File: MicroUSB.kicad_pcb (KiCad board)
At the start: 2 copper layers, 13.8 x 16.1 mm, 11 parts, among them J1 USB_OTG, J2 Conn_01x05, Q1 MMBT3904, U1 USBLC6-2SC6

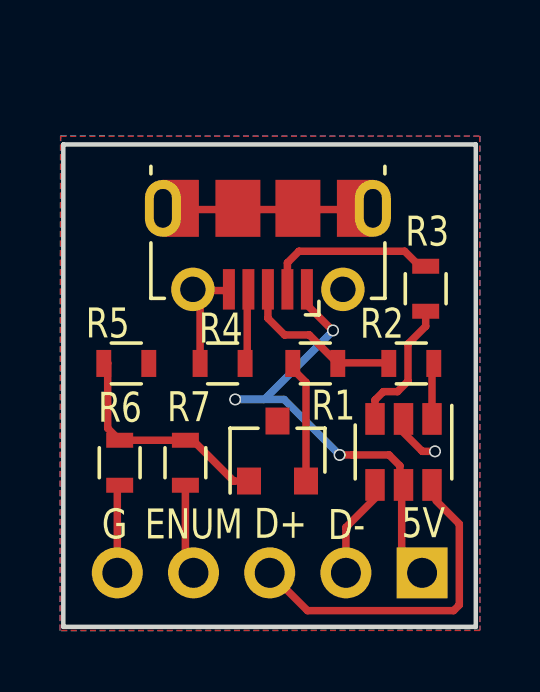
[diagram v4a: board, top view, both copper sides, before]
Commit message: Added a txt V.01 indicated version 1 and added gerber file for panelizing
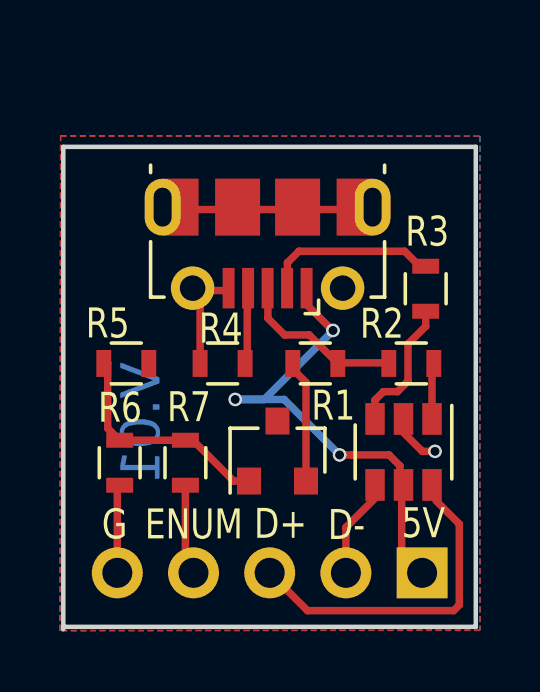
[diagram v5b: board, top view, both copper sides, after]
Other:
- outline, holes or cut-outs redrawn
- net class new added: clearance 0.2, trace_width 0.25, via_dia 0.453, via_drill 0.3
- board text added: "Micro_USB_Conn"
- board text added: "V.01"
- board text removed: "Micro_USB_Connector"
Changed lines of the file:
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@@
     (links 29)
     (no_connects 0)
-    (area 145.684999 109.545 160.555 127.795001)
+    (area 136.700001 107.04 160.555 127.795001)
     (thickness 1.6)
-    (drawings 27)
+    (drawings 28)
     (tracks 85)
     (zones 0)
@@
     (pad_drill 0.85)
     (pad_to_mask_clearance 0.2)
-    (aux_axis_origin 0 0)
+    (aux_axis_origin 144.76 110.82)
     (visible_elements 7FFFFFFF)
     (pcbplotparams
-      (layerselection 0x00030_80000001)
-      (usegerberextensions false)
+      (layerselection 0x0ffff_80000001)
+      (usegerberextensions true)
+      (usegerberattributes true)
       (excludeedgelayer true)
       (linewidth 0.100000)
@@
       (viasonmask false)
       (mode 1)
-      (useauxorigin false)
+      (useauxorigin true)
       (hpglpennumber 1)
       (hpglpenspeed 20)
@@
       (psa4output false)
       (plotreference true)
-      (plotvalue true)
+      (plotvalue false)
       (plotinvisibletext false)
       (padsonsilk false)
@@
       (outputformat 1)
       (mirror false)
-      (drillshape 1)
+      (drillshape 0)
       (scaleselection 1)
-      (outputdirectory ""))
+      (outputdirectory GERBER_MUSB/))
   )
   (net 0 "")
@@
     (add_net "Net-(R3-Pad1)")
   )
+  (net_class new ""
+    (clearance 0.2)
+    (trace_width 0.25)
+    (via_dia 0.453)
+    (via_drill 0.3)
+    (uvia_dia 0.3)
+    (uvia_drill 0.1)
+  )
   (module Connectors_USB:USB_Micro-B_Molex-105017-0001 (layer F.Cu)
-    (at 152.72 113.97 180)
+    (at 152.71 113.93 180)
     (descr http://www.molex.com/pdm_docs/sd/1050170001_sd.pdf)
     (tags "Micro-USB SMD Typ-B")
@@
     )
   )
-  (dimension 16.08 (width 0.3) (layer Eco1.User)
-    (gr_text "16.080 mm" (at 143.2 119.53 270) (layer Eco1.User)
+  (gr_text V.01 (at 148.5 120.77 90) (layer B.Cu)
+    (effects (font (size 1.3 1.3) (thickness 0.325)) (justify mirror))
+  )
+  (dimension 16 (width 0.3) (layer Eco1.User)
+    (gr_text "16.000 mm" (at 143.2 119.57 270) (layer Eco1.User)
       (effects (font (size 1.5 1.5) (thickness 0.3)))
     )
     (feature1 (pts (xy 145.9 127.57) (xy 141.85 127.57)))
-    (feature2 (pts (xy 145.9 111.49) (xy 141.85 111.49)))
-    (crossbar (pts (xy 144.55 111.49) (xy 144.55 127.57)))
+    (feature2 (pts (xy 145.9 111.57) (xy 141.85 111.57)))
+    (crossbar (pts (xy 144.55 111.57) (xy 144.55 127.57)))
     (arrow1a (pts (xy 144.55 127.57) (xy 143.963579 126.443496)))
     (arrow1b (pts (xy 144.55 127.57) (xy 145.136421 126.443496)))
-    (arrow2a (pts (xy 144.55 111.49) (xy 143.963579 112.616504)))
-    (arrow2b (pts (xy 144.55 111.49) (xy 145.136421 112.616504)))
+    (arrow2a (pts (xy 144.55 111.57) (xy 143.963579 112.696504)))
+    (arrow2b (pts (xy 144.55 111.57) (xy 145.136421 112.696504)))
   )
   (dimension 13.75 (width 0.3) (layer Eco1.User)
@@
     (arrow2b (pts (xy 145.9 109.74) (xy 147.026504 109.153579)))
   )
-  (gr_line (start 145.9 127.57) (end 145.9 111.49) (layer Edge.Cuts) (width 0.15))
-  (gr_line (start 159.65 127.57) (end 159.65 111.49) (layer Edge.Cuts) (width 0.15))
+  (gr_line (start 145.9 127.65) (end 145.9 111.57) (layer Edge.Cuts) (width 0.15))
+  (gr_line (start 159.65 127.57) (end 159.65 111.57) (layer Edge.Cuts) (width 0.15))
   (gr_line (start 145.9 127.57) (end 159.65 127.57) (layer Edge.Cuts) (width 0.15))
-  (gr_line (start 159.65 111.49) (end 145.9 111.49) (layer Edge.Cuts) (width 0.15))
-  (gr_text Micro_USB_Connector (at 152.82 123.61) (layer B.SilkS)
-    (effects (font (size 0.5 0.5) (thickness 0.125)) (justify mirror))
-  )
-  (gr_line (start 151.91 122.6) (end 151.25 123.04) (layer B.SilkS) (width 0.2))
-  (gr_line (start 151.77 122.34) (end 151.01 122.53) (layer B.SilkS) (width 0.2))
-  (gr_line (start 151.69 122.08) (end 150.99 121.98) (layer B.SilkS) (width 0.2))
-  (gr_line (start 153.61 122.53) (end 154.13 122.97) (layer B.SilkS) (width 0.2))
-  (gr_line (start 153.69 122.27) (end 154.37 122.38) (layer B.SilkS) (width 0.2))
-  (gr_line (start 153.7 122.01) (end 154.44 121.8) (layer B.SilkS) (width 0.2))
-  (gr_line (start 152.43 122.71) (end 152.96 122.32) (layer B.SilkS) (width 0.2))
-  (gr_line (start 152.46 122.3) (end 153.01 122.67) (layer B.SilkS) (width 0.2))
-  (gr_circle (center 153.05 121.57) (end 153.12 121.49) (layer B.SilkS) (width 0.2))
-  (gr_circle (center 152.29 121.57) (end 152.39 121.53) (layer B.SilkS) (width 0.2))
-  (gr_line (start 151.39 120.41) (end 151.56 121.19) (layer B.SilkS) (width 0.2))
-  (gr_line (start 152.02 120.81) (end 151.41 120.42) (layer B.SilkS) (width 0.2))
-  (gr_line (start 154.21 120.47) (end 153.84 121.29) (layer B.SilkS) (width 0.2))
-  (gr_line (start 153.4 120.85) (end 154.2 120.47) (layer B.SilkS) (width 0.2))
-  (gr_circle (center 152.68 121.91) (end 153.68 121.16) (layer B.SilkS) (width 0.2))
+  (gr_line (start 159.65 111.57) (end 145.9 111.57) (layer Edge.Cuts) (width 0.15))
+  (gr_text Micro_USB_Conn (at 152.82 123.61) (layer B.SilkS)
+    (effects (font (size 1 0.8) (thickness 0.2)) (justify mirror))
+  )
+  (gr_line (start 151.94 122.16) (end 151.28 122.6) (layer B.SilkS) (width 0.2))
+  (gr_line (start 151.72 121.85) (end 150.96 122.04) (layer B.SilkS) (width 0.2))
+  (gr_line (start 151.7 121.47) (end 151 121.37) (layer B.SilkS) (width 0.2))
+  (gr_line (start 153.5 122.18) (end 154.02 122.62) (layer B.SilkS) (width 0.2))
+  (gr_line (start 153.73 121.95) (end 154.41 122.06) (layer B.SilkS) (width 0.2))
+  (gr_line (start 153.74 121.62) (end 154.48 121.41) (layer B.SilkS) (width 0.2))
+  (gr_line (start 152.52 122.11) (end 153.05 121.72) (layer B.SilkS) (width 0.2))
+  (gr_line (start 152.53 121.72) (end 153.08 122.09) (layer B.SilkS) (width 0.2))
+  (gr_circle (center 153.13 121.03) (end 153.2 120.95) (layer B.SilkS) (width 0.2))
+  (gr_circle (center 152.36 121.04) (end 152.46 121) (layer B.SilkS) (width 0.2))
+  (gr_line (start 151.34 120.12) (end 151.51 120.9) (layer B.SilkS) (width 0.2))
+  (gr_line (start 151.98 120.49) (end 151.37 120.1) (layer B.SilkS) (width 0.2))
+  (gr_line (start 154.18 120.04) (end 153.81 120.86) (layer B.SilkS) (width 0.2))
+  (gr_line (start 153.38 120.42) (end 154.18 120.04) (layer B.SilkS) (width 0.2))
+  (gr_circle (center 152.72 121.48) (end 153.72 120.73) (layer B.SilkS) (width 0.2))
   (gr_text G (at 147.61 124.16) (layer F.SilkS)
     (effects (font (size 1 0.8) (thickness 0.2)))
@@
   (segment (start 157.12 120.974264) (end 157.865736 121.72) (width 0.25) (layer F.Cu) (net 1))
   (segment (start 157.12 120.78) (end 157.12 120.974264) (width 0.25) (layer F.Cu) (net 1))
-  (via (at 158.29 121.72) (size 0.4) (drill 0.3) (layers F.Cu B.Cu) (net 1))
+  (via (at 158.29 121.72) (size 0.453) (drill 0.3) (layers F.Cu B.Cu) (net 1))
   (segment (start 150.46 118.77) (end 150.46 116.6) (width 0.25) (layer F.Cu) (net 1))
   (segment (start 150.46 116.6) (end 150.22 116.36) (width 0.25) (layer F.Cu) (net 1))
@@
   (segment (start 155.11 121.84) (end 153.26 119.99) (width 0.25) (layer B.Cu) (net 3))
   (segment (start 153.26 119.99) (end 151.63 119.99) (width 0.25) (layer B.Cu) (net 3))
-  (via (at 151.63 119.99) (size 0.4) (drill 0.3) (layers F.Cu B.Cu) (net 3))
+  (via (at 151.63 119.99) (size 0.453) (drill 0.3) (layers F.Cu B.Cu) (net 3))
   (segment (start 154.02 116.835) (end 154.875004 117.690004) (width 0.25) (layer F.Cu) (net 3))
   (segment (start 154.02 116.36) (end 154.02 116.835) (width 0.25) (layer F.Cu) (net 3))
   (segment (start 154.875004 117.690004) (end 154.89 117.690004) (width 0.25) (layer F.Cu) (net 3))
-  (via (at 154.89 117.690004) (size 0.4) (drill 0.3) (layers F.Cu B.Cu) (net 3))
+  (via (at 154.89 117.690004) (size 0.453) (drill 0.3) (layers F.Cu B.Cu) (net 3))
   (segment (start 157.12 122.2) (end 156.76 121.84) (width 0.25) (layer F.Cu) (net 3))
   (segment (start 157.12 122.98) (end 157.12 122.2) (width 0.25) (layer F.Cu) (net 3))
   (segment (start 155.534264 121.84) (end 155.11 121.84) (width 0.25) (layer F.Cu) (net 3))
   (segment (start 156.76 121.84) (end 155.534264 121.84) (width 0.25) (layer F.Cu) (net 3))
-  (via (at 155.11 121.84) (size 0.4) (drill 0.3) (layers F.Cu B.Cu) (net 3))
+  (via (at 155.11 121.84) (size 0.453) (drill 0.3) (layers F.Cu B.Cu) (net 3))
   (segment (start 157.12 122.98) (end 157.18 123.04) (width 0.25) (layer F.Cu) (net 3))
   (segment (start 157.18 123.04) (end 157.18 125.09) (width 0.25) (layer F.Cu) (net 3))

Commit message: Created a new microUSB footprint and replaced the old one
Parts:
- J1: footprint Connectors_USB:USB_Micro-B_Molex-105017-0001 -> MicroUSB:MicroUSB(SMD)
- moved J1 1.39 mm to (152.7, 115.3), turned to 0 degrees
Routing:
- net GND: track 15.3 -> 26.0 mm, vias 1 -> 2
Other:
- board size 13.8 x 16.1 mm -> 13.8 x 16 mm

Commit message: Changed the clearance of coppoer pour to 0.3mm and changed the footprint of micro usb
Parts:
- added Kitty: G***, Logo:Kitty, B.Cu at (153.3, 121.0)
- J1: footprint MicroUSB:MicroUSB(SMD) -> Connectors_USB:USB_Micro-B_Molex-105017-0001
- moved J1 1.45 mm to (152.7, 113.9), turned to 180 degrees
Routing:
- net GND: track 26.0 -> 29.1 mm

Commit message: Moved the micro USB out 0.7mm from edge to edge
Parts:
- moved J1 0.25 mm to (152.7, 113.6)
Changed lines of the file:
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@@
     (links 29)
     (no_connects 0)
-    (area 145.824999 111.494999 159.725001 127.645001)
+    (area 136.700001 107.04 160.555 127.795001)
     (thickness 1.6)
     (drawings 13)
-    (tracks 106)
+    (tracks 109)
     (zones 0)
     (modules 12)
@@
     (tags "resistor 0603")
     (attr smd)
-    (fp_text reference R2 (at 0.98 1.32 180) (layer F.SilkS)
+    (fp_text reference R2 (at 1.04 1.24 180) (layer F.SilkS)
       (effects (font (size 0.85 0.85) (thickness 0.2)))
     )
@@
     (tags "resistor 0603")
     (attr smd)
-    (fp_text reference R4 (at -0.06 -1.16) (layer F.SilkS)
+    (fp_text reference R4 (at -0.06 -1.21) (layer F.SilkS)
       (effects (font (size 0.85 0.85) (thickness 0.2)))
     )
@@
   )
   (module Connectors_USB:USB_Micro-B_Molex-105017-0001 (layer F.Cu)
-    (at 152.7 113.87 180)
+    (at 152.72 113.62 180)
     (descr http://www.molex.com/pdm_docs/sd/1050170001_sd.pdf)
     (tags "Micro-USB SMD Typ-B")
@@
     (effects (font (size 0.85 0.85) (thickness 0.2)))
   )
+  (segment (start 150.43 116.72) (end 150.43 118.76) (width 0.25) (layer F.Cu) (net 1))
+  (segment (start 150.43 116.72) (end 150.43 116.18) (width 0.25) (layer F.Cu) (net 1))
+  (segment (start 150.43 116.45) (end 150.43 116.72) (width 0.25) (layer F.Cu) (net 1))
+  (segment (start 150.43 116.18) (end 150.22 115.97) (width 0.25) (layer F.Cu) (net 1))
+  (segment (start 155.22 115.97) (end 155.22 115.99) (width 0.25) (layer F.Cu) (net 1))
+  (segment (start 155.22 115.99) (end 155.49 116.26) (width 0.25) (layer F.Cu) (net 1))
+  (segment (start 155.49 116.26) (end 157.599681 116.26) (width 0.25) (layer F.Cu) (net 1))
+  (segment (start 157.599681 116.26) (end 157.92 116.26) (width 0.25) (layer F.Cu) (net 1))
+  (segment (start 153.7 113.28) (end 151.7 113.28) (width 0.25) (layer F.Cu) (net 1))
+  (segment (start 155.6 113.28) (end 153.7 113.28) (width 0.25) (layer F.Cu) (net 1))
+  (segment (start 156.2 113.28) (end 155.6 113.28) (width 0.25) (layer F.Cu) (net 1))
+  (segment (start 157.92 116.26) (end 158.63 116.26) (width 0.25) (layer F.Cu) (net 1))
+  (segment (start 158.63 116.26) (end 158.87 116.02) (width 0.25) (layer F.Cu) (net 1))
+  (segment (start 158.87 116.02) (end 158.87 114.684592) (width 0.25) (layer F.Cu) (net 1))
+  (segment (start 158.87 114.684592) (end 157.465408 113.28) (width 0.25) (layer F.Cu) (net 1))
+  (segment (start 157.465408 113.28) (end 156.2 113.28) (width 0.25) (layer F.Cu) (net 1))
+  (segment (start 149.8 113.28) (end 151.7 113.28) (width 0.25) (layer F.Cu) (net 1))
+  (segment (start 149.2 113.28) (end 149.8 113.28) (width 0.25) (layer F.Cu) (net 1))
+  (segment (start 149.2 113.28) (end 149.2 114.48) (width 0.25) (layer F.Cu) (net 1))
+  (segment (start 149.2 114.48) (end 149.205 114.485) (width 0.25) (layer F.Cu) (net 1))
+  (segment (start 149.205 114.485) (end 149.205 115.235) (width 0.25) (layer F.Cu) (net 1))
+  (segment (start 151.4 115.98) (end 150.2 115.98) (width 0.25) (layer F.Cu) (net 1))
   (segment (start 150.2 116.22) (end 150.43 116.45) (width 0.25) (layer F.Cu) (net 1))
-  (segment (start 150.43 116.45) (end 150.43 118.76) (width 0.25) (layer F.Cu) (net 1))
   (segment (start 150.43 118.76) (end 150.46 118.79) (width 0.25) (layer F.Cu) (net 1))
-  (segment (start 149.81 113.65) (end 149.21 113.65) (width 0.25) (layer F.Cu) (net 1))
-  (segment (start 155.61 113.65) (end 156.21 113.65) (width 0.25) (layer F.Cu) (net 1))
-  (segment (start 157.01 113.684592) (end 156.495 113.684592) (width 0.25) (layer F.Cu) (net 1))
-  (segment (start 157.87 113.684592) (end 157.01 113.684592) (width 0.25) (layer F.Cu) (net 1))
-  (segment (start 157.01 113.684592) (end 156.244592 113.684592) (width 0.25) (layer F.Cu) (net 1))
   (segment (start 156.244592 113.684592) (end 156.21 113.65) (width 0.25) (layer F.Cu) (net 1))
   (segment (start 155.21 116.35) (end 155.29 116.27) (width 0.25) (layer F.Cu) (net 1))
-  (segment (start 155.29 116.27) (end 157.91 116.27) (width 0.25) (layer F.Cu) (net 1))
   (segment (start 157.91 116.27) (end 157.92 116.26) (width 0.25) (layer F.Cu) (net 1))
-  (segment (start 150.21 116.35) (end 151.41 116.35) (width 0.25) (layer F.Cu) (net 1))
   (segment (start 150.21 116.35) (end 150.21 116.24) (width 0.25) (layer F.Cu) (net 1))
   (segment (start 150.21 116.24) (end 149.205 115.235) (width 0.25) (layer F.Cu) (net 1))
   (segment (start 149.205 115.235) (end 149.21 115.23) (width 0.25) (layer F.Cu) (net 1))
-  (segment (start 149.21 115.23) (end 149.21 113.65) (width 0.25) (layer F.Cu) (net 1))
   (segment (start 155.62 113.66) (end 156.22 113.66) (width 0.25) (layer F.Cu) (net 1))
-  (segment (start 153.72 113.66) (end 155.62 113.66) (width 0.25) (layer F.Cu) (net 1))
-  (segment (start 151.72 113.66) (end 153.72 113.66) (width 0.25) (layer F.Cu) (net 1))
-  (segment (start 149.82 113.66) (end 151.72 113.66) (width 0.25) (layer F.Cu) (net 1))
-  (segment (start 149.22 113.66) (end 149.82 113.66) (width 0.25) (layer F.Cu) (net 1))
-  (segment (start 157.92 116.26) (end 158.63 116.26) (width 0.25) (layer F.Cu) (net 1))
   (via (at 157.92 116.26) (size 0.453) (drill 0.3) (layers F.Cu B.Cu) (net 1))
-  (segment (start 158.63 116.26) (end 158.87 116.02) (width 0.25) (layer F.Cu) (net 1))
-  (segment (start 158.87 116.02) (end 158.87 114.684592) (width 0.25) (layer F.Cu) (net 1))
-  (segment (start 158.87 114.684592) (end 157.87 113.684592) (width 0.25) (layer F.Cu) (net 1))
-  (segment (start 148.76999 113.8464) (end 148.76999 113.684592) (width 0.25) (layer F.Cu) (net 1))
-  (segment (start 150.46 116.6) (end 150.035408 116.6) (width 0.25) (layer F.Cu) (net 1))
   (segment (start 157.865736 121.72) (end 158.29 121.72) (width 0.25) (layer F.Cu) (net 1))
   (segment (start 157.12 120.974264) (end 157.865736 121.72) (width 0.25) (layer F.Cu) (net 1))
@@
   (segment (start 147.7 125.77) (end 147.7 122.93) (width 0.25) (layer F.Cu) (net 1))
   (segment (start 147.7 122.93) (end 147.78 122.85) (width 0.25) (layer F.Cu) (net 1))
-  (segment (start 153.37 116.36) (end 153.37 115.435) (width 0.25) (layer F.Cu) (net 2))
-  (segment (start 153.37 115.435) (end 153.755 115.05) (width 0.25) (layer F.Cu) (net 2))
-  (segment (start 153.755 115.05) (end 157.28 115.05) (width 0.25) (layer F.Cu) (net 2))
-  (segment (start 157.28 115.05) (end 157.78 115.55) (width 0.25) (layer F.Cu) (net 2))
-  (segment (start 157.78 115.55) (end 157.98 115.55) (width 0.25) (layer F.Cu) (net 2))
+  (segment (start 157.98 115.55) (end 157.78 115.55) (width 0.25) (layer F.Cu) (net 2))
+  (segment (start 157.78 115.55) (end 156.96 114.73) (width 0.25) (layer F.Cu) (net 2))
+  (segment (start 156.96 114.73) (end 153.63 114.73) (width 0.25) (layer F.Cu) (net 2))
+  (segment (start 153.63 114.73) (end 153.35 115.01) (width 0.25) (layer F.Cu) (net 2))
+  (segment (start 153.35 115.01) (end 153.35 115.98) (width 0.25) (layer F.Cu) (net 2))
   (segment (start 154.02 116.835) (end 154.875004 117.690004) (width 0.25) (layer F.Cu) (net 3))
   (segment (start 154.02 116.36) (end 154.02 116.835) (width 0.25) (layer F.Cu) (net 3))
